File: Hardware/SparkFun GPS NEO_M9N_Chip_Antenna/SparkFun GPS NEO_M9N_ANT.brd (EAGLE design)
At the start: 40.6 x 33 mm, 91 parts, among them J2 Qwiic Right Angle, J4 Qwiic Right Angle, U1 U-BLOX_NEO-M9N, U2 3.3V, Y1 GPS_CHIP_ANTENNAW3011

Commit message: Adds sweet silk to Antenna design
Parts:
- added U$21: (no value), NEO_GPS_board_silk_FINAL#03#jpg:NEO_GPS_BOARD_SILK_FINAL#03#JPG
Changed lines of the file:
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@@
 </element>
 <element name="U$13" library="ANT" package="ANT0" value="" x="37.5412" y="20.2184" smashed="yes" rot="R90"/>
+<element name="U$21" library="NEO_GPS_board_silk_FINAL#03#jpg" package="NEO_GPS_BOARD_SILK_FINAL#03#JPG" value="" x="15.24" y="11.43" smashed="yes" rot="MR0"/>
 </elements>
 <signals>

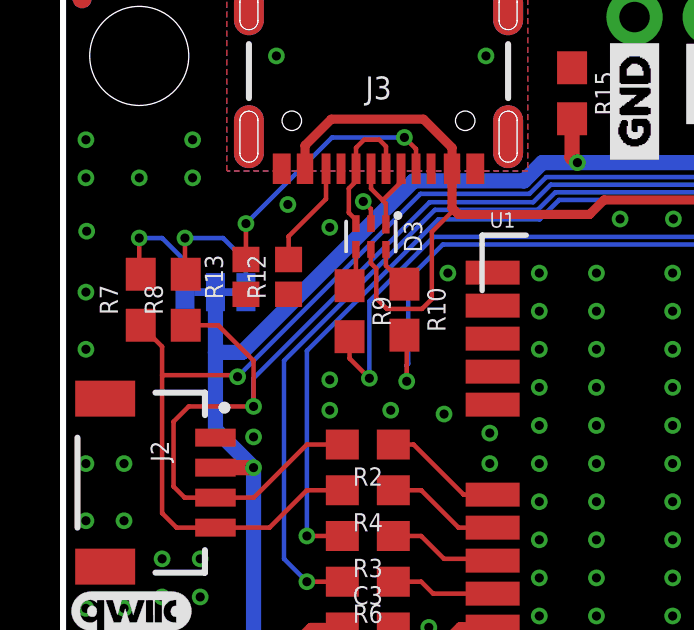
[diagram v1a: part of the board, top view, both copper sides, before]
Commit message: Updates both designs with 5.1k resistor in 0603 package
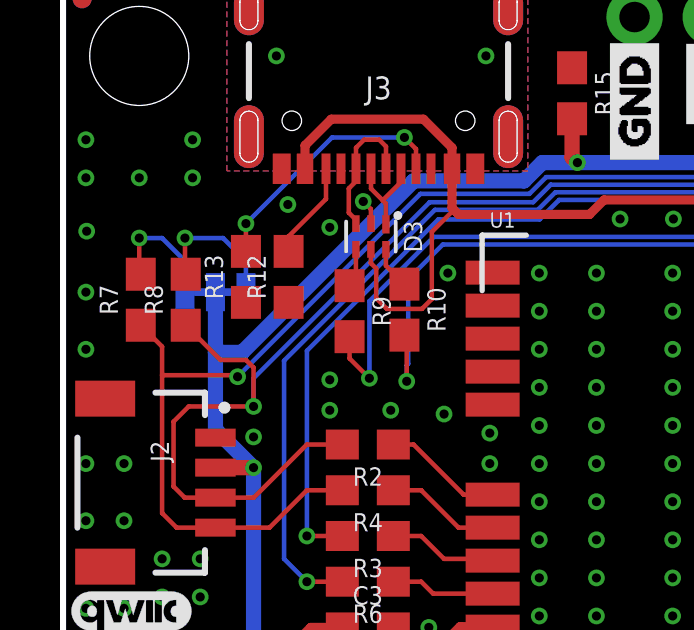
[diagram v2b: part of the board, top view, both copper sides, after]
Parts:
- R12, R13: device SparkFun-Resistors:0402 -> SparkFun-Resistors:0603
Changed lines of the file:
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@@
 <attribute name="VALUE" x="10.5156" y="30.6578" size="0.762" layer="27" rot="R180" align="center"/>
 </element>
-<element name="R12" library="SparkFun-Resistors" package="0402" value="5.1k" x="7.5184" y="23.0886" smashed="yes" rot="R90">
+<element name="R12" library="SparkFun-Resistors" package="0603" value="5.1k" x="7.5184" y="23.0886" smashed="yes" rot="R90">
 <attribute name="NAME" x="6.7564" y="23.0886" size="0.6096" layer="25" font="vector" ratio="20" rot="R90" align="bottom-center"/>
-<attribute name="PROD_ID" value="RES-14340" x="7.5184" y="23.0886" size="1.778" layer="27" font="vector" ratio="15" rot="R90" display="off"/>
+<attribute name="PROD_ID" value="RES-12083" x="7.5184" y="23.0886" size="1.778" layer="27" font="vector" ratio="15" rot="R90" display="off"/>
 <attribute name="VALUE" x="8.2804" y="23.0886" size="0.6096" layer="27" font="vector" ratio="20" rot="R90" align="top-center"/>
 </element>
-<element name="R13" library="SparkFun-Resistors" package="0402" value="5.1k" x="6.096" y="23.0886" smashed="yes" rot="R90">
+<element name="R13" library="SparkFun-Resistors" package="0603" value="5.1k" x="6.096" y="23.0886" smashed="yes" rot="R90">
 <attribute name="NAME" x="5.334" y="23.0886" size="0.6096" layer="25" font="vector" ratio="20" rot="R90" align="bottom-center"/>
-<attribute name="PROD_ID" value="RES-14340" x="6.096" y="23.0886" size="1.778" layer="27" font="vector" ratio="15" rot="R90" display="off"/>
+<attribute name="PROD_ID" value="RES-12083" x="6.096" y="23.0886" size="1.778" layer="27" font="vector" ratio="15" rot="R90" display="off"/>
 <attribute name="VALUE" x="6.858" y="23.0886" size="0.6096" layer="27" font="vector" ratio="20" rot="R90" align="top-center"/>
 </element>
@@
 <contactref element="J5" pad="3"/>
 <wire x1="31.4452" y1="3.5052" x2="29.21" y2="1.27" width="0.1524" layer="1"/>
-<wire x1="6.35" y1="20.2946" x2="5.168" y2="21.4766" width="0.1524" layer="1"/>
-<wire x1="6.35" y1="20.2946" x2="6.35" y2="18.7706" width="0.1524" layer="1"/>
 <wire x1="5.08" y1="15.7306" x2="4.056" y2="15.7306" width="0.1524" layer="1"/>
 <wire x1="4.056" y1="15.7306" x2="3.683" y2="16.1036" width="0.1524" layer="1"/>
 <wire x1="5.08" y1="15.7306" x2="6.358" y2="15.7306" width="0.1524" layer="1"/>
 <contactref element="R8" pad="1"/>
-<wire x1="5.168" y1="21.4766" x2="4.0894" y2="21.4766" width="0.1524" layer="1"/>
 <wire x1="16.256" y1="26.162" x2="24.0792" y2="26.162" width="0.1524" layer="16"/>
 <wire x1="24.3332" y1="26.416" x2="24.0792" y2="26.162" width="0.1524" layer="16"/>
@@
 <wire x1="26.6827" y1="31.7373" x2="26.67" y2="31.75" width="0.1524" layer="16"/>
 <wire x1="26.6827" y1="28.7655" x2="26.6827" y2="31.7373" width="0.1524" layer="16"/>
+<wire x1="4.0894" y1="21.4766" x2="5.246" y2="20.32" width="0.1524" layer="1"/>
+<wire x1="5.246" y1="20.32" x2="6.096" y2="20.32" width="0.1524" layer="1"/>
+<wire x1="6.096" y1="20.32" x2="6.35" y2="20.066" width="0.1524" layer="1"/>
+<wire x1="6.35" y1="20.066" x2="6.35" y2="18.7706" width="0.1524" layer="1"/>
 </signal>
 <signal name="!RESET">
@@
 <contactref element="J3" pad="B5"/>
 <wire x1="8.7656" y1="25.6862" x2="8.7656" y2="26.6938" width="0.1524" layer="1"/>
-<wire x1="7.5184" y1="23.6686" x2="7.5184" y2="24.439" width="0.1524" layer="1"/>
+<wire x1="7.5184" y1="23.9386" x2="7.5184" y2="24.439" width="0.1524" layer="1"/>
 <wire x1="7.5184" y1="24.439" x2="8.7656" y2="25.6862" width="0.1524" layer="1"/>
 </signal>
@@
 <wire x1="8.9662" y1="27.7368" x2="6.096" y2="24.8666" width="0.1524" layer="16"/>
 <via x="6.096" y="24.8666" extent="1-16" drill="0.3048"/>
-<wire x1="6.096" y1="24.8666" x2="6.096" y2="23.6686" width="0.1524" layer="1"/>
+<wire x1="6.096" y1="24.8666" x2="6.096" y2="23.9386" width="0.1524" layer="1"/>
 </signal>
 </signals>

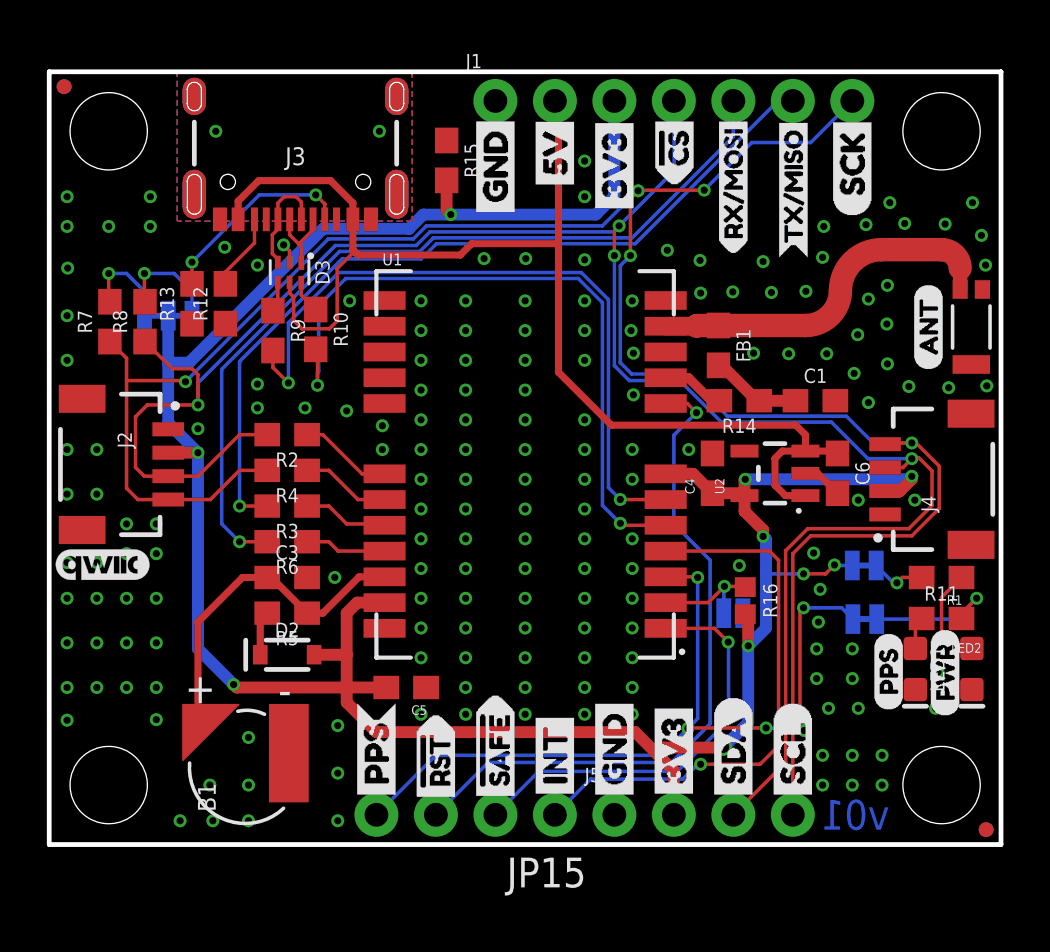
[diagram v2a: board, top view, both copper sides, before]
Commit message: Updates the antenna version to have better ground pour on the antenna, and a better curve on the feed line
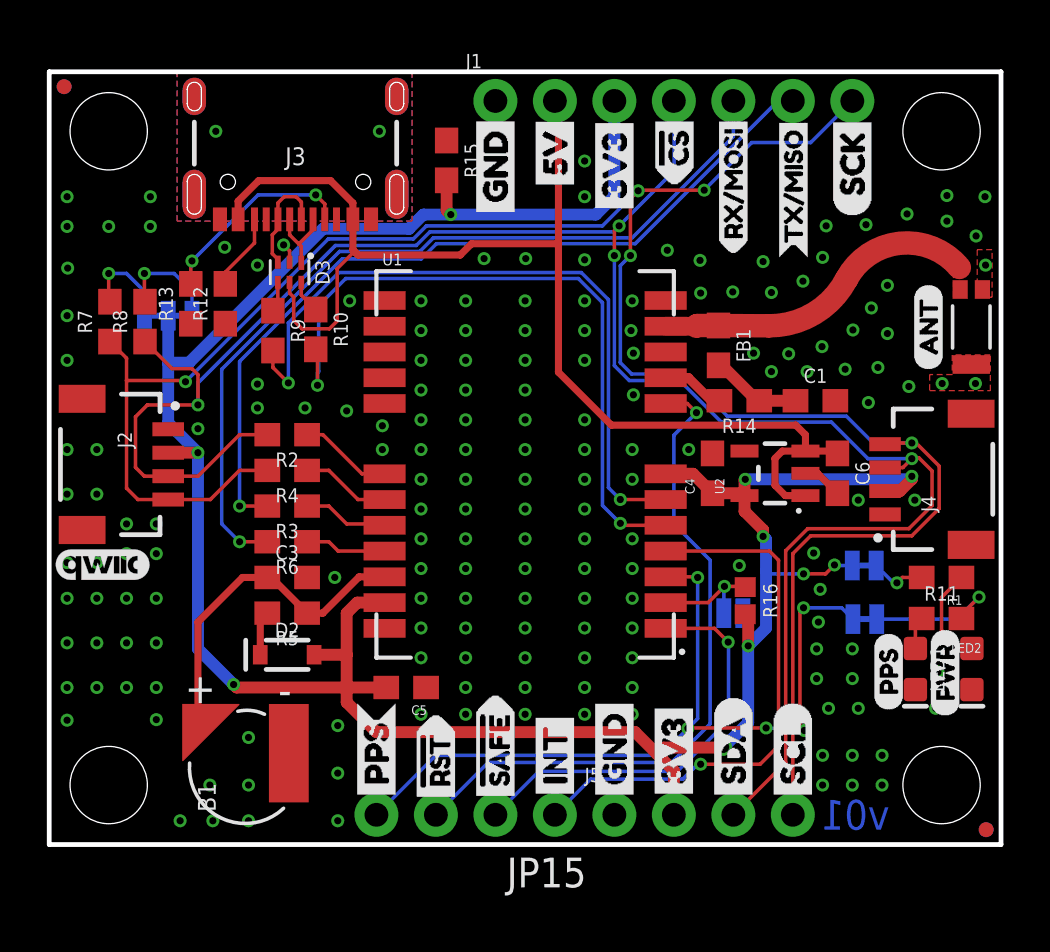
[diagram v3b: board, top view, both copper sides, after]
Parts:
- moved R13 0.05 mm to (6.05, 23.1)
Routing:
- net GPS_ANT1: track 15.2 -> 13.1 mm
- net GND: vias 179 -> 181
- added copper zone on layer 1, net GPS_ANT1

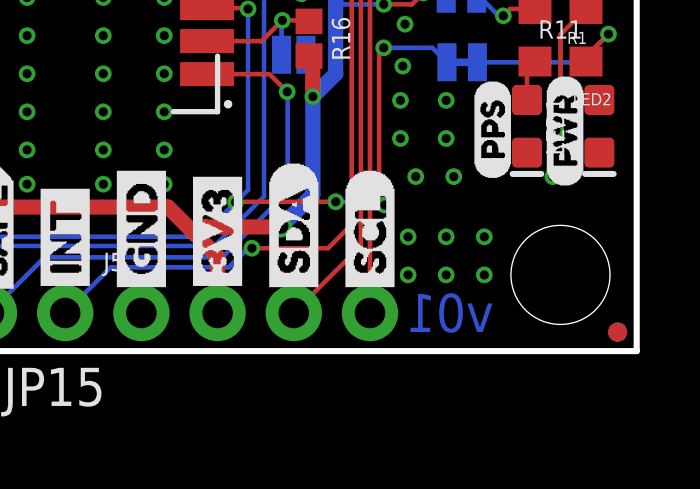
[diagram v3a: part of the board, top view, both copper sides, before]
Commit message: Changes version to v02
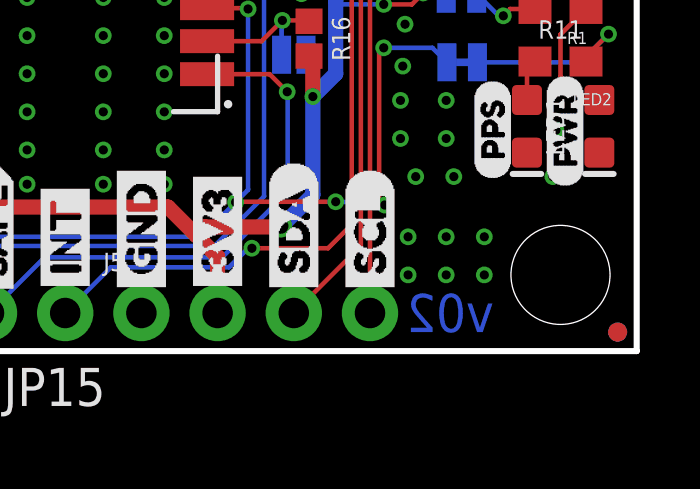
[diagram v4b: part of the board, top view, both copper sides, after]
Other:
- board text added: "v02"
- board text removed: "v01"
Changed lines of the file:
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@@
 <wire x1="40.64" y1="32.9946" x2="40.64" y2="0" width="0.2032" layer="20"/>
 <wire x1="40.64" y1="0" x2="0" y2="0" width="0.2032" layer="20"/>
-<text x="34.417" y="1.27" size="1.27" layer="16" font="vector" ratio="15" rot="MR180" align="center">v01</text>
+<text x="34.417" y="1.27" size="1.27" layer="16" font="vector" ratio="15" rot="MR180" align="center">v02</text>
 <text x="-2.54" y="-8.89" size="1.778" layer="47">Measurements in inches</text>
 <dimension x1="0" y1="0" x2="0" y2="33.02" x3="-7.62" y3="16.51" textsize="1.778" textratio="15" layer="47" unit="inch"/>

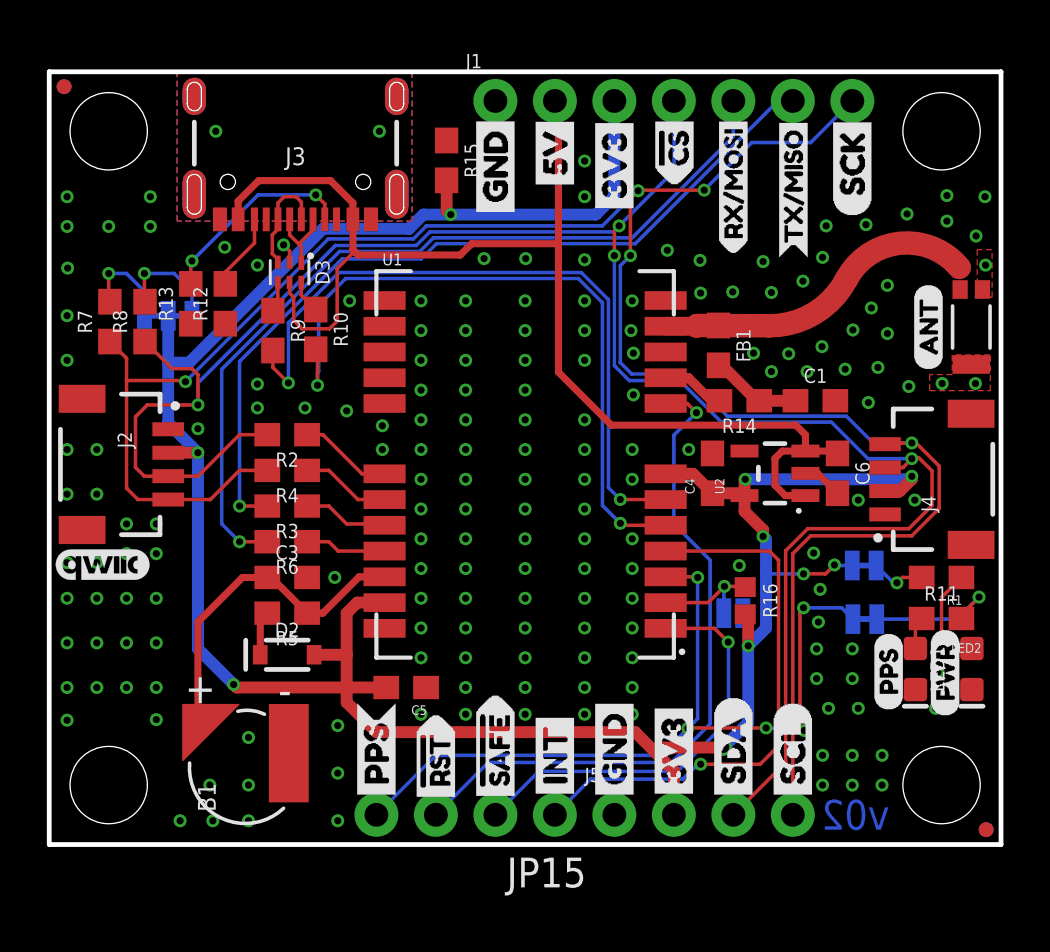
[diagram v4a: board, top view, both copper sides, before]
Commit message: Removes VCC bias to antenna from antenna design
* Deletes all gerber files related to prototypes
* Moves GPS library out of the buzzard label folder
* Deletes buzzard labels
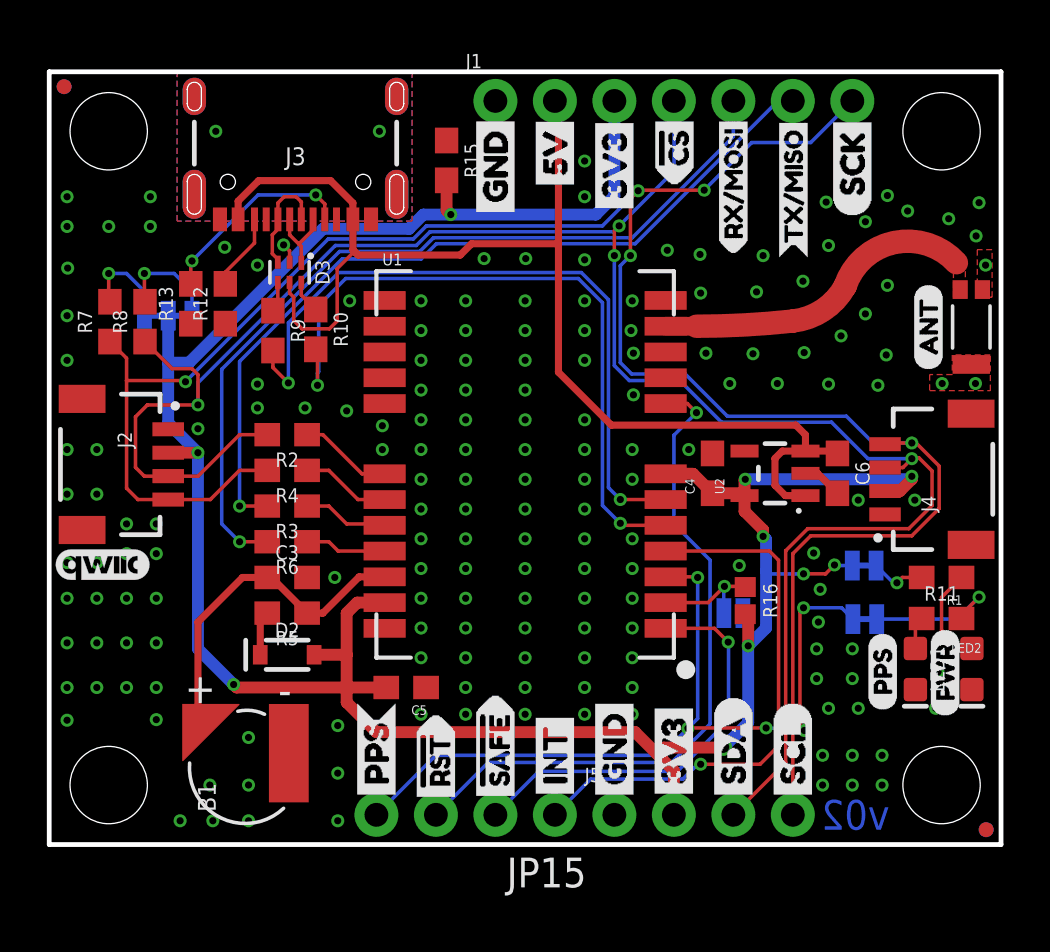
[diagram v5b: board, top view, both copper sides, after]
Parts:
- removed C1: 47pF, SparkFun-Capacitors:0603
- removed FB1: 30Ω/1.8A, SparkFun-Coils:0603
- removed R14: 10, SparkFun-Resistors:0603
- moved U$52 0.25 mm to (35.6, 5.71)
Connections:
- removed net ANT_VCC: C1.1, FB1.2, R14.1
- net GND: no longer C1.2
- net GPS_ANT1: no longer FB1.1
- net VCC_RF: no longer R14.2
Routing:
- net ANT_VCC: track 5.47 -> 0.00 mm
- net VCC_RF: track 2.70 -> 0.00 mm
- net GND: vias 181 -> 178

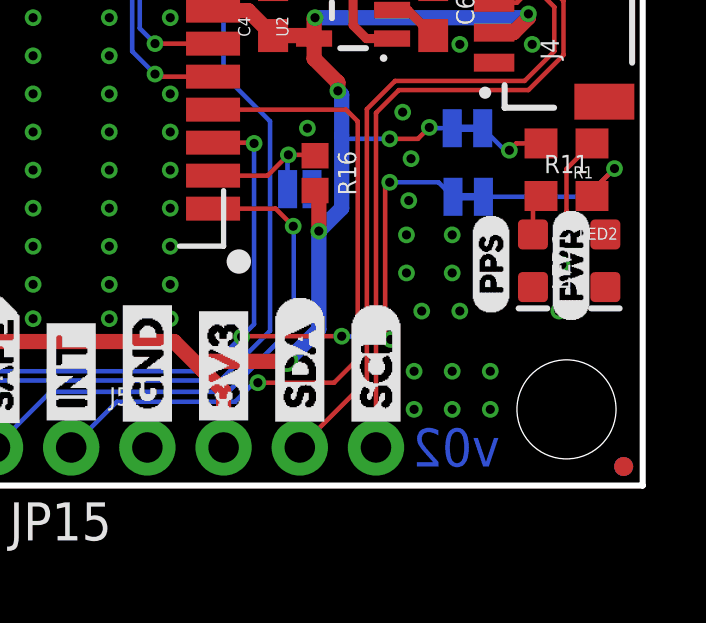
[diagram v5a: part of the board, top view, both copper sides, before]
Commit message: Updates Schematic to be more neat
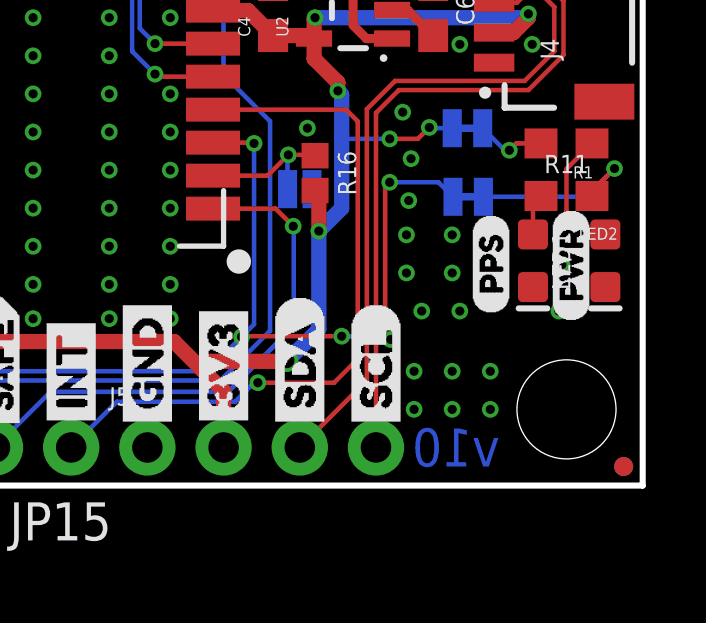
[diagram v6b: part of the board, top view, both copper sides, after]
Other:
- board text added: "v10"
- board text removed: "v02"
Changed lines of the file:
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@@
 <layer number="19" name="Unrouted" color="6" fill="1" visible="yes" active="yes"/>
 <layer number="20" name="Dimension" color="15" fill="1" visible="yes" active="yes"/>
-<layer number="21" name="tPlace" color="16" fill="1" visible="yes" active="yes"/>
-<layer number="22" name="bPlace" color="14" fill="1" visible="yes" active="yes"/>
+<layer number="21" name="tPlace" color="16" fill="1" visible="no" active="yes"/>
+<layer number="22" name="bPlace" color="14" fill="1" visible="no" active="yes"/>
 <layer number="23" name="tOrigins" color="15" fill="1" visible="yes" active="yes"/>
 <layer number="24" name="bOrigins" color="15" fill="1" visible="yes" active="yes"/>
@@
 <layer number="37" name="tTest" color="7" fill="1" visible="no" active="yes"/>
 <layer number="38" name="bTest" color="7" fill="1" visible="no" active="yes"/>
-<layer number="39" name="tKeepout" color="4" fill="11" visible="yes" active="yes"/>
+<layer number="39" name="tKeepout" color="4" fill="11" visible="no" active="yes"/>
 <layer number="40" name="bKeepout" color="1" fill="11" visible="no" active="yes"/>
 <layer number="41" name="tRestrict" color="4" fill="10" visible="no" active="yes"/>
@@
 <wire x1="40.64" y1="32.9946" x2="40.64" y2="0" width="0.2032" layer="20"/>
 <wire x1="40.64" y1="0" x2="0" y2="0" width="0.2032" layer="20"/>
-<text x="34.417" y="1.27" size="1.27" layer="16" font="vector" ratio="15" rot="MR180" align="center">v02</text>
+<text x="34.417" y="1.27" size="1.27" layer="16" font="vector" ratio="15" rot="MR180" align="center">v10</text>
 <text x="-2.54" y="-8.89" size="1.778" layer="47">Measurements in inches</text>
 <dimension x1="0" y1="0" x2="0" y2="33.02" x3="-7.62" y3="16.51" textsize="1.778" textratio="15" layer="47" unit="inch"/>
@@
 <contactref element="C3" pad="2"/>
 <contactref element="B1" pad="-"/>
-<contactref element="LED1" pad="C"/>
 <polygon width="0.254" layer="1" rank="2">
 <vertex x="0" y="32.9946"/>
@@
 </polygon>
 <contactref element="C4" pad="2"/>
-<contactref element="LED2" pad="C"/>
 <contactref element="C5" pad="1"/>
 <contactref element="U2" pad="2"/>
@@
 <via x="39.5478" y="19.685" extent="1-16" drill="0.3048"/>
 <via x="29.0576" y="19.685" extent="1-16" drill="0.3048"/>
+<contactref element="LED1" pad="C"/>
+<contactref element="LED2" pad="C"/>
 </signal>
 <signal name="SCL/SCK">
@@
 <wire x1="13.97" y1="1.27" x2="16.51" y2="3.81" width="0.1524" layer="16"/>
 <wire x1="16.51" y1="3.81" x2="26.1181125" y2="3.81" width="0.1524" layer="16"/>
-<wire x1="33.8328" y1="10.1092" x2="32.2072" y2="10.1092" width="0.1524" layer="16"/>
+<wire x1="32.2072" y1="10.1092" x2="33.8328" y2="10.1092" width="0.1524" layer="16"/>
 <via x="32.2072" y="10.1092" extent="1-16" drill="0.3048"/>
 <wire x1="34.3154" y1="9.6266" x2="33.8328" y2="10.1092" width="0.1524" layer="16"/>
